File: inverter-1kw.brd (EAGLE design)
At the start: 97.8 x 100.1 mm, 189 parts, among them IC1 LMV358MMX, IC2 LMV358MMX, Q4 1200980569**TRANS SMD NPN MMB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, Q6 1200980569**TRANS SMD NPN MMB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, U1 ACS712, U4 ACS712, U5 SI8230, U6 SI8230, U7 ACS712

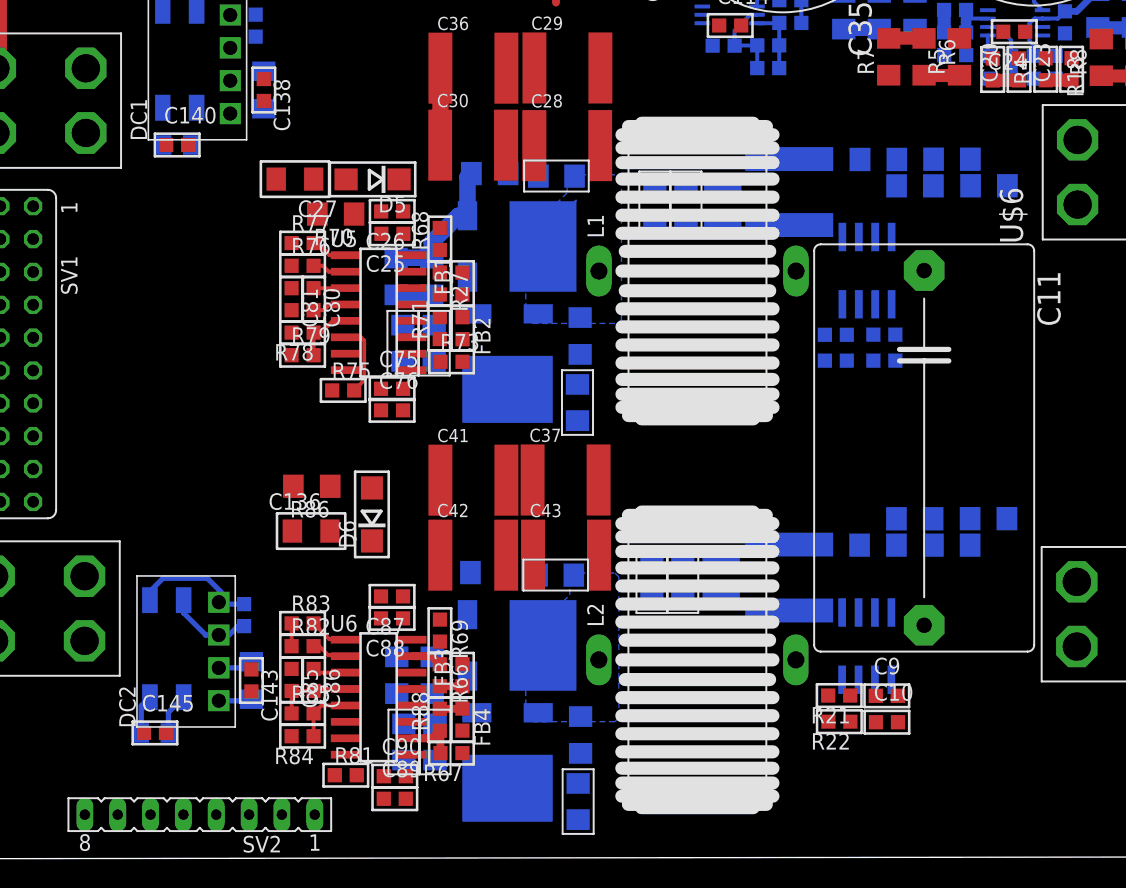
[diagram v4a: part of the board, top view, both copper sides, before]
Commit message: Soket baglantilari duzenlendi. B kol mosfetin AGND baglantisi duzeltildi.
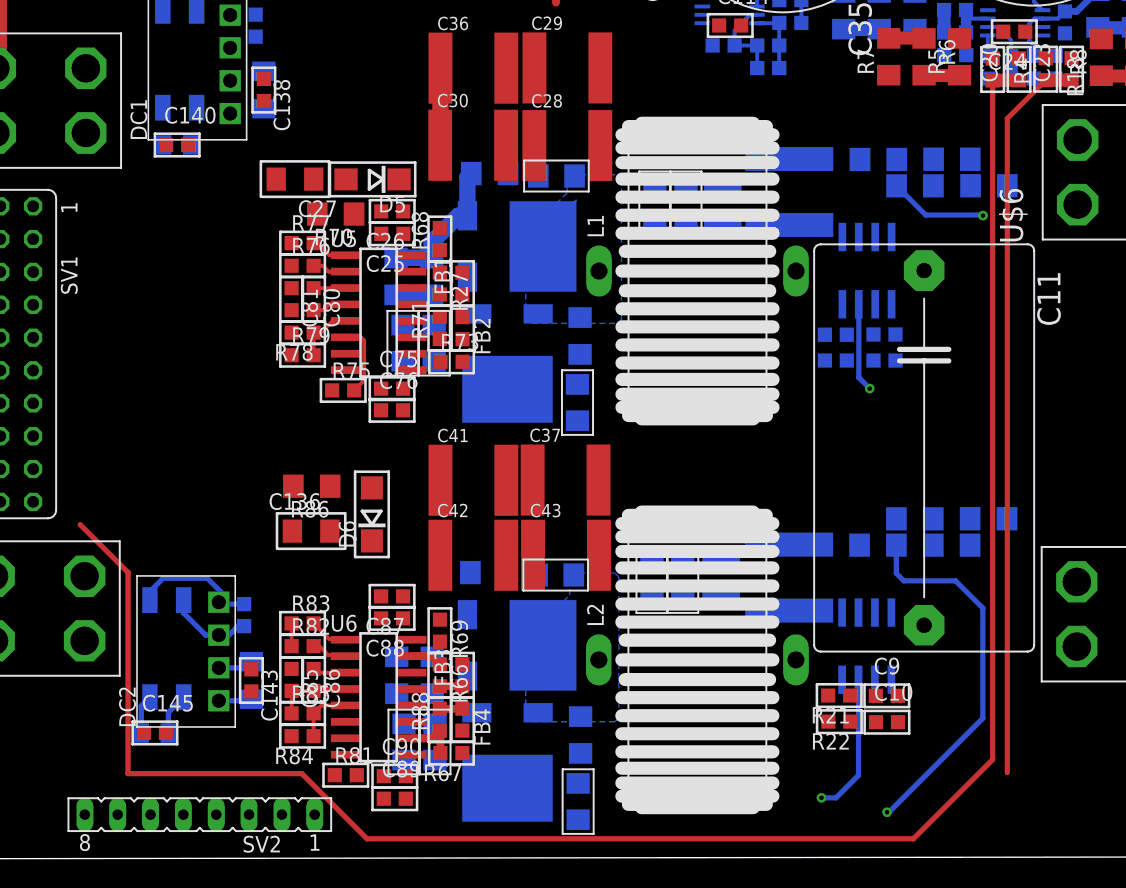
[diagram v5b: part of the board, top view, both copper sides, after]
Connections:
- removed net FAN: SV1.14
- removed net N$39: C32.-, C33.-, C35.-, C37.2, C40.-, C43.2, C47.2, C48.2, C49.2, C89.2, C90.2, GN4.S, LED5.C, R28.1, R67.1, R96.1, RGND1.2, U$5.1, U$5.2, U$5.3, U$5.4, U6.9
- removed net N$83: R78.1, R79.2, U5.5
- removed net N$88: R84.1, R85.2, U6.5
- removed net NTC-HS1: SV1.16
- removed net NTC-HS2: SV1.18
- new net DRV1_EN: R78.1, R79.2, SV1.9, U5.5
- new net DRV2_EN: R84.1, R85.2, SV1.15, U6.5
- new net N$38: SV1.8
- net +3V3: now also SV1.17
- net +5V: now also SV1.19
- net AGND: now also C32.-, C33.-, C35.-, C37.2, C40.-, C43.2, C47.2, C48.2, C49.2, C89.2, C90.2, GN4.S, LED5.C, R28.1, R67.1, R96.1, RGND1.2, U$5.1, U$5.2, U$5.3, U$5.4, U6.9
- net DGND: now also SV1.20
- net G11_PWM: now also SV1.5; no longer SV1.2
- net G12_PWM: now also SV1.7; no longer SV1.4
- net G13_PWM: now also SV1.11; no longer SV1.6
- net G14_PWM: now also SV1.13; no longer SV1.8
- net IA_SENS: now also SV1.14; no longer SV1.9
- net IB_SENS: now also SV1.18; no longer SV1.11
- net IIN_SENS: now also SV1.3; no longer SV1.5
- net RELAY1: now also SV1.2; no longer SV1.10
- net RELAY2: now also SV1.4; no longer SV1.12
- net VA_SENS: now also SV1.12; no longer SV1.13
- net VB_SENS: now also SV1.16; no longer SV1.15
- net VIN_SENS: now also SV1.1; no longer SV1.7
- net VIN_SENS_DIFF: now also SV1.10; no longer SV1.3
- net VOUT_SENS_DIFF: now also SV1.6; no longer SV1.1
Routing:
- net VIN_SENS_DIFF: track 2.04 -> 146.9 mm
- net VA_SENS: track 0.00 -> 142.1 mm, vias 0 -> 1
- net IA_SENS: track 0.00 -> 128.6 mm, vias 0 -> 1
- net VB_SENS: track 0.00 -> 108.9 mm, vias 0 -> 1
- net IB_SENS: track 0.00 -> 85.4 mm, vias 0 -> 1
- net VOUT_SENS_DIFF: track 2.00 -> 56.8 mm
- net N$83: track 4.56 -> 0.00 mm
- net DRV1_EN: track 0.00 -> 4.56 mm
- net N$88: track 4.44 -> 0.00 mm
- net DRV2_EN: track 0.00 -> 4.44 mm
- net N$39: track 2.38 -> 0.00 mm
- net AGND: track 0.00 -> 2.38 mm
- added copper zone on layer 1, net AGND
- removed copper zone on layer 1, net N$39

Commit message: Düzenlemeler yapıldı.
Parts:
- moved LED5 9.76 mm to (61.0, 107.5), turned to 180 degrees
- moved R86 8.38 mm to (29.6, 20.6)
- moved RGND 4.45 mm to (34.4, 107.1)
- moved D6 3.17 mm to (32.7, 23.5), turned to 180 degrees
- moved R101 2.95 mm to (60.4, 62.8)
- moved C19 2.93 mm to (60.4, 61.1)
- moved SV2 2.89 mm to (16.7, 2.39)
- moved RGND1 2.66 mm to (41.1, 105.7)
- moved C136 2.45 mm to (26.5, 23.4), turned to 180 degrees
- moved R100 0.55 mm to (60.4, 62.7), flipped to the top, turned to 180 degrees
- moved C4 0.45 mm to (59.9, 50.8)
- moved R7 0.43 mm to (72.2, 62.0)
- moved C1 0.42 mm to (65.1, 51.2)
- moved R6 0.41 mm to (75.0, 62.0)
- moved R5 0.40 mm to (77.7, 62.0)
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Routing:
- net VB_OUT: track 0.00 -> 78.0 mm
- net VOUT_SENS_DIFF: track 56.8 -> 109.4 mm, vias 0 -> 1
- net IB_SENS: track 85.4 -> 46.3 mm, vias 1 -> 0
- net VA_SENS: track 142.1 -> 103.6 mm, vias 1 -> 2
- net VIN_SENS_DIFF: track 146.9 -> 110.3 mm, vias 0 -> 1
- net +3V3: track 0.00 -> 30.8 mm, vias 0 -> 1
- net VA_OUT: track 0.00 -> 26.6 mm
- net DGND: track 37.8 -> 62.0 mm, vias 2 -> 6
- net AGND: track 2.38 -> 18.7 mm
- net N$9: track 5.19 -> 17.6 mm, vias 0 -> 1
- net IA_SENS: track 128.6 -> 139.7 mm, vias 1 -> 4
- net N$20: track 3.73 -> 12.0 mm, vias 0 -> 1
- net VCC_2: track 3.05 -> 10.7 mm
- net N$95: track 0.00 -> 7.55 mm
- net N$18: track 1.65 -> 9.18 mm, vias 0 -> 1
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- added copper zone on layer 16, net AGND
- added copper zone on layer 16, net VA_FILTER
- added copper zone on layer 16, net VA_OUT
- added copper zone on layer 16, net VB_FILTER
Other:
- board size 97.8 x 100.1 mm -> 105.8 x 104.1 mm

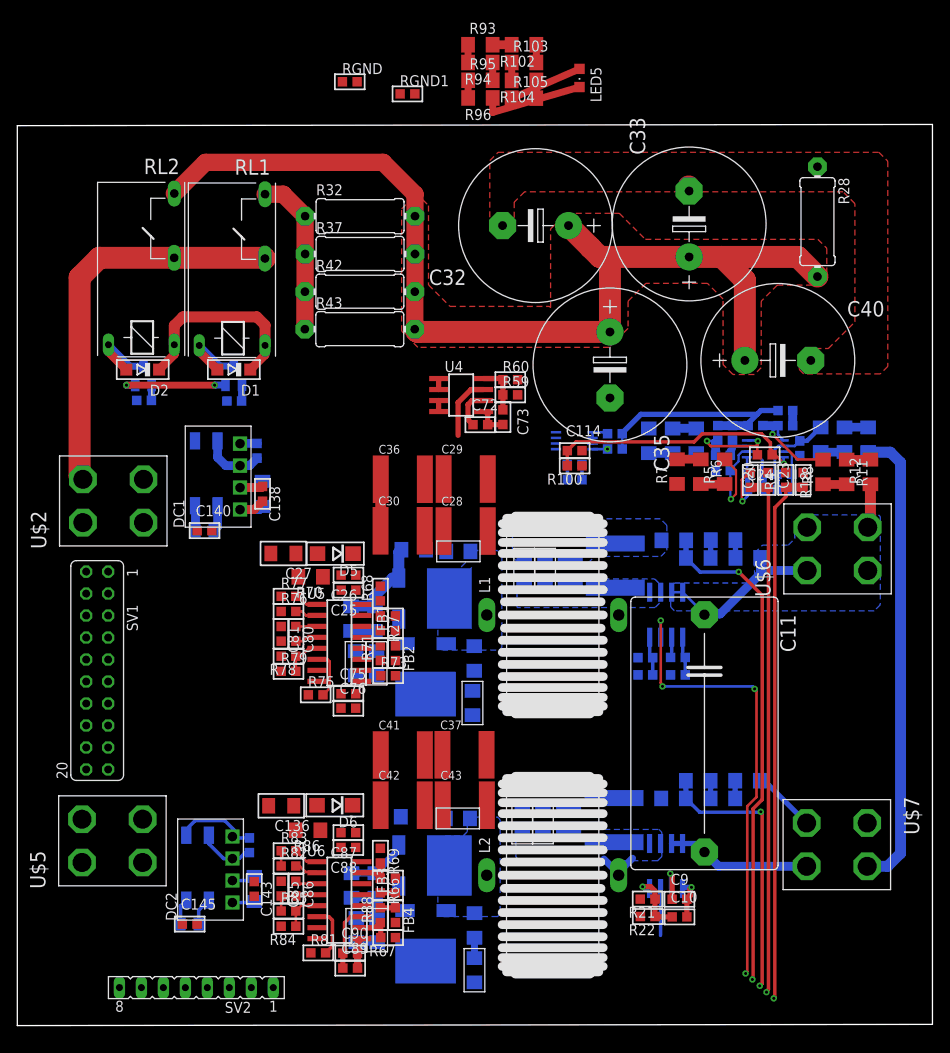
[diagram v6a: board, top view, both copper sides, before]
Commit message: ölçüm devresi düzenlendi
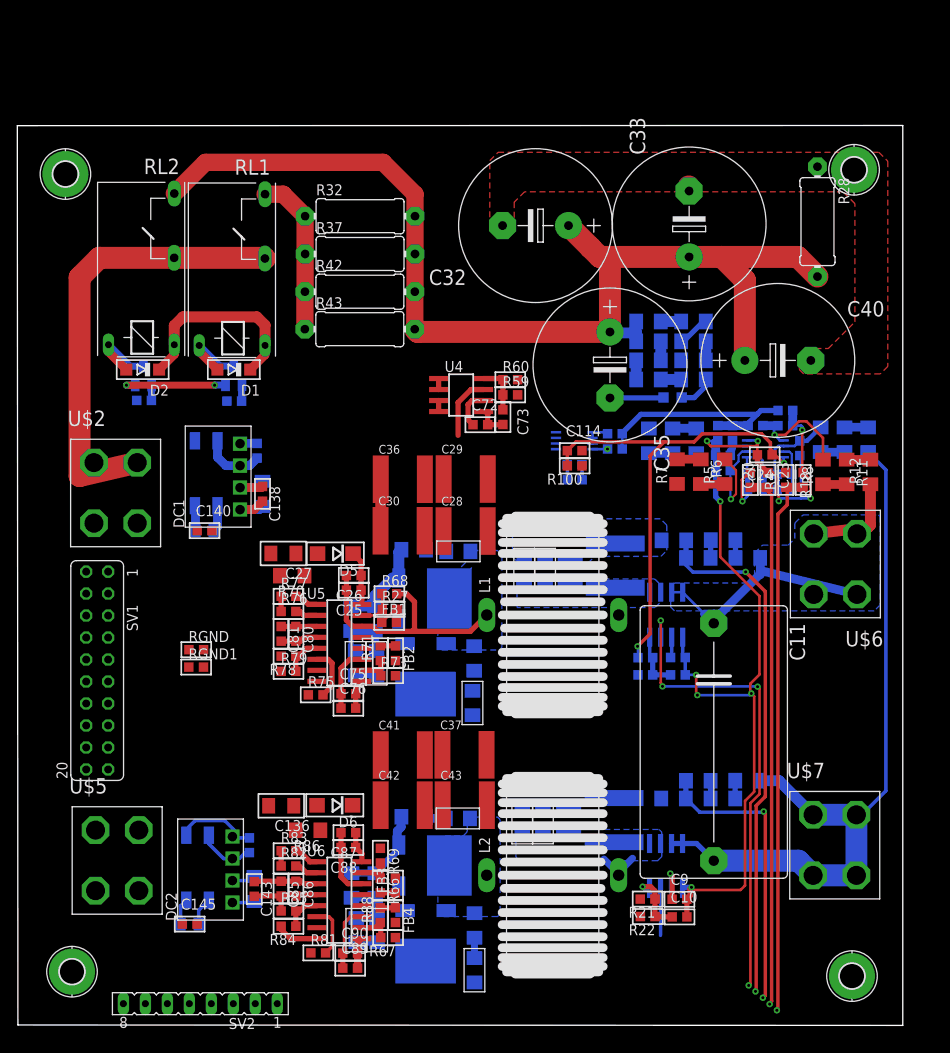
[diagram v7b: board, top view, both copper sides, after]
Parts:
- added H1, H2, H3, H4: MOUNT-PAD-ROUND2.8, holes:2,8-PAD
- moved RGND1 70.6 mm to (16.7, 39.4)
- moved RGND 68.0 mm to (16.7, 41.4)
- moved R96 39.1 mm to (74.1, 74.9), flipped to the bottom
- moved R95 38.9 mm to (74.1, 77.1), flipped to the bottom
- moved R94 38.8 mm to (74.1, 79.4), flipped to the bottom, turned to 0 degrees
- moved LED5 38.5 mm to (71.7, 70.6), flipped to the bottom, turned to 270 degrees
- moved R105 38.0 mm to (74.1, 72.7), flipped to the bottom
- moved R104 37.4 mm to (68.9, 72.7), flipped to the bottom, turned to 0 degrees
- moved R93 37.4 mm to (68.9, 79.4), flipped to the bottom
- moved R103 37.3 mm to (68.9, 74.9), flipped to the bottom, turned to 180 degrees
- moved R102 37.2 mm to (68.9, 77.1), flipped to the bottom, turned to 0 degrees
- moved U$5 2.60 mm to (7.69, 17.0), turned to 0 degrees
- moved R70 2.13 mm to (27.8, 50.0)
- moved R27 1.94 mm to (39.0, 46.1), turned to 0 degrees
- moved SV2 1.92 mm to (17.1, 0.53)
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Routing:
- net DGND: track 62.0 -> 163.8 mm, vias 6 -> 13
- net IB_SENS: track 46.3 -> 5.43 mm
- net IA_SENS: track 139.7 -> 99.8 mm
- net SW_LEG_A: track 7.14 -> 35.8 mm
- net +3V3: track 30.8 -> 56.9 mm, vias 1 -> 2
- net VB_SENS: track 101.4 -> 79.9 mm
- net VA_OUT: track 26.6 -> 40.0 mm
- net +5V: track 13.3 -> 24.8 mm
- net VB_OUT: track 78.0 -> 88.3 mm
- net VDDA: track 0.00 -> 9.94 mm
- net SW_LEG_B: track 0.00 -> 7.84 mm
- net VCC_1: track 2.90 -> 10.4 mm
- net VSUPPLY+: track 46.3 -> 52.6 mm
- net N$79: track 2.76 -> 7.68 mm
- net N$68: track 8.57 -> 4.11 mm
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- removed copper zone on layer 1, net V_IN
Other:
- board size 105.8 x 104.1 mm -> 102.3 x 104 mm

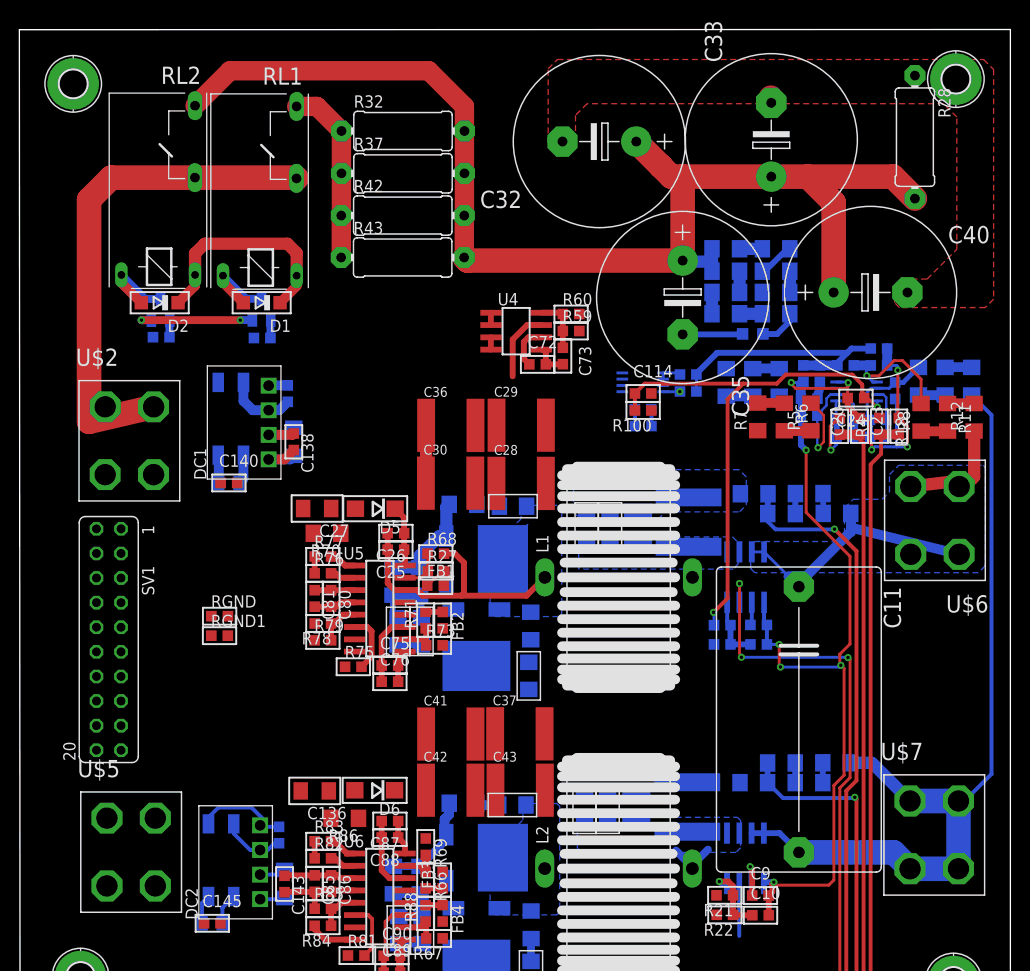
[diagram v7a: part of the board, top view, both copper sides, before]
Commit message: Giris ve giris terminalleri soket yapildi. Ganlarin dibindeki capler sadelestirildi.
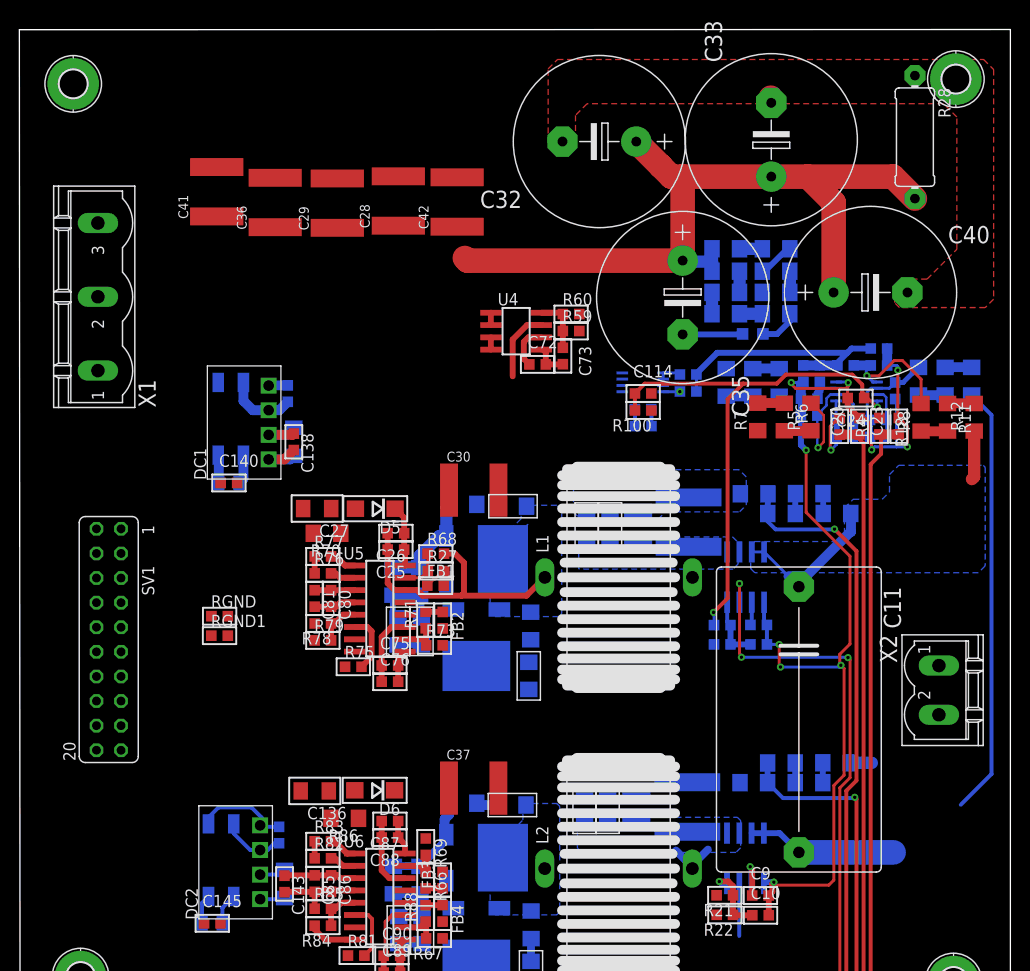
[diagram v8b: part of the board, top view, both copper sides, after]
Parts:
- removed C43: (no value), rcl:C2220K
- removed D1, D2: (no value), diode:SOD123
- removed Q4, Q6: 1200980569**TRANS SMD NPN MMBTA06 SOT-23 80V 500mA, transistor-npn:SOT23
- removed R32, R37, R42, R43: (no value), rcl:0411/12
- removed R36, R41: (no value), rcl:R0603
- removed RL1, RL2: 0417, Erelay:0417
- removed U$2, U$5, U$6, U$7: (no value), Andromeda:SCREWCONNECTORS(K93-01AH)
- added X1: GMSTBV3, con-phoenix-762:GMSTBV3
- added X2: MSTBV2, con-phoenix-508:MSTBV2
- moved C41 61.0 mm to (16.4, 85.3), turned to 90 degrees
- moved C42 60.7 mm to (41.2, 84.2), turned to 90 degrees
- moved C28 31.8 mm to (35.1, 84.3), turned to 90 degrees
- moved C29 29.8 mm to (28.8, 84.1), turned to 90 degrees
- moved C36 29.3 mm to (22.4, 84.2), turned to 90 degrees
- moved C37 7.36 mm to (42.9, 23.7)
- moved C30 2.50 mm to (42.9, 54.5)
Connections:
- removed net N$14: C42.2, C43.1
- removed net N$22: C28.1, C30.2
- removed net N$32: C29.1, C36.2
- removed net N$33: C37.1, C41.2
- removed net N$44: D1.A, Q4.3, RL1.2
- removed net N$45: Q4.1, R36.1
- removed net N$51: D2.A, Q6.3, RL2.2
- removed net N$52: Q6.1, R41.1
- removed net N$55: R32.1, R37.1, R42.1, R43.1, RL1.S
- removed net V_IN: C32.+, C33.+, C35.+, C40.+, R102.2, R28.2, R32.2, R37.2, R42.2, R43.2, R93.2, RL2.S, U4.1, U4.2
- new net PE: H1.B2,8, H2.B2,8, H3.B2,8, H4.B2,8, X1.1
- net AGND: now also C30.2, C36.2, C41.2, C42.2, X1.3; no longer C43.2, U$5.1, U$5.2, U$5.3, U$5.4
- net DGND: no longer Q4.2, Q6.2
- net RELAY1: no longer R36.2
- net RELAY2: no longer R41.2
- net VA_OUT: now also X2.1; no longer U$6.1, U$6.2, U$6.3, U$6.4
- net VB_OUT: now also X2.2; no longer U$7.1, U$7.2, U$7.3, U$7.4
- net VDD: no longer D1.C, D2.C, RL1.1, RL2.1
- net VIN: now also C37.1; no longer C36.1, C41.1, C42.1
- net VSUPPLY+: now also C28.1, C29.1, C32.+, C33.+, C35.+, C36.1, C40.+, C41.1, C42.1, R102.2, R28.2, R93.2, U4.1, U4.2, X1.2; no longer RL1.O, RL2.O, U$2.1, U$2.2, U$2.3, U$2.4
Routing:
- net V_IN: track 128.7 -> 0.00 mm
- net VSUPPLY+: track 52.6 -> 82.3 mm
- net VB_OUT: track 88.3 -> 62.8 mm
- net VDD: track 23.0 -> 0.00 mm
- net N$55: track 18.8 -> 0.00 mm
- net VA_OUT: track 40.0 -> 22.1 mm
- net DGND: track 163.8 -> 151.4 mm, vias 13 -> 11
- net N$51: track 8.80 -> 0.00 mm
- net N$44: track 8.63 -> 0.00 mm
- net VIN: track 28.8 -> 22.9 mm
- net N$45: track 1.87 -> 0.00 mm
- net N$52: track 1.76 -> 0.00 mm
